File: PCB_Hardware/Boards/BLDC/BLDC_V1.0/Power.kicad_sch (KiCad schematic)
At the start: 43 parts, among them J3 Conn_01x02_Pin, J4 Conn_01x02_Pin, Q13 IPT015N10N5, Q2 IPT015N10N5, U11 AMS1117-3.3, U5 LM5069MM-2, U6 TLV70233_SOT23-5

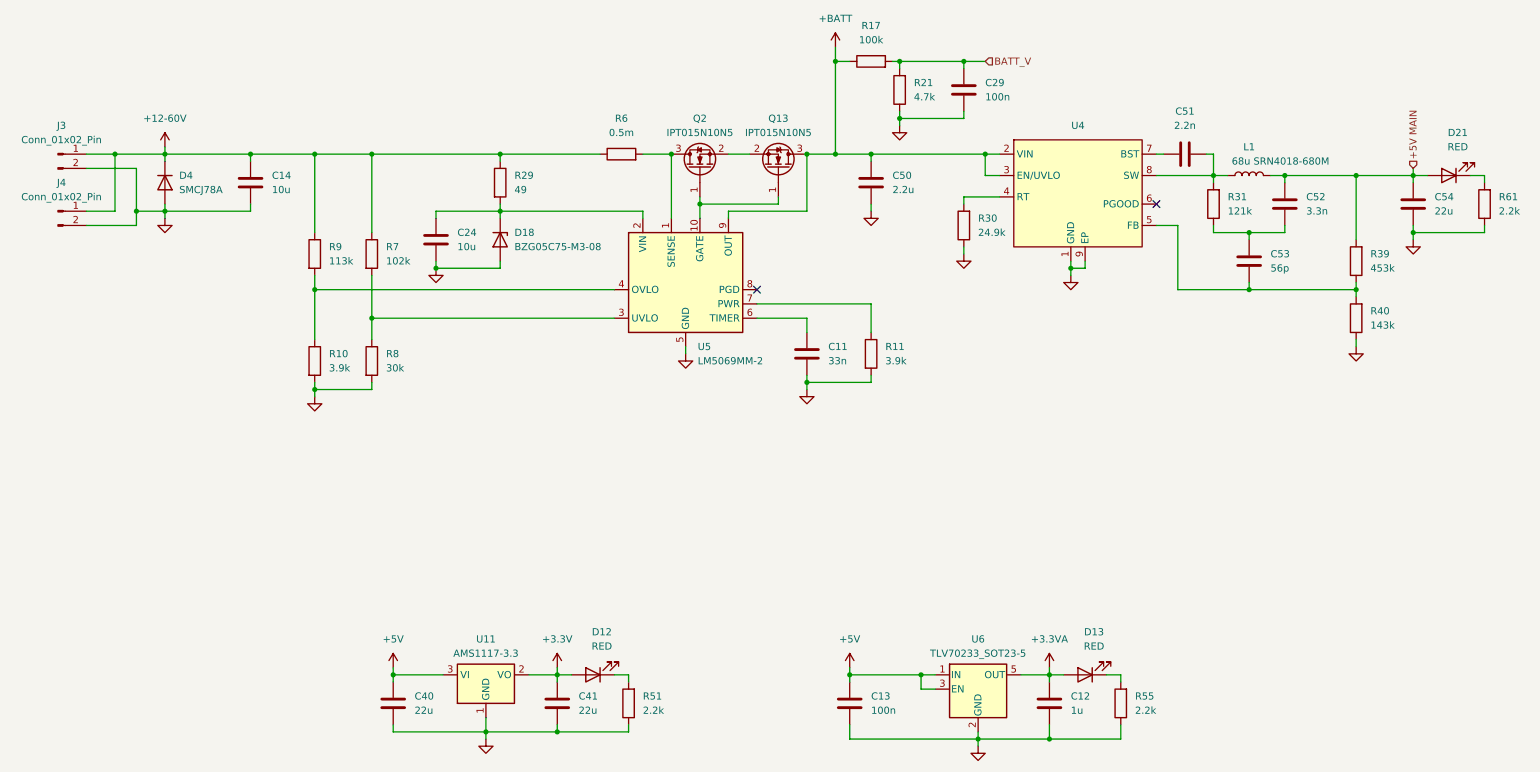
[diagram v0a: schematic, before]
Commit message: minor BLDC changes and production files for ordering
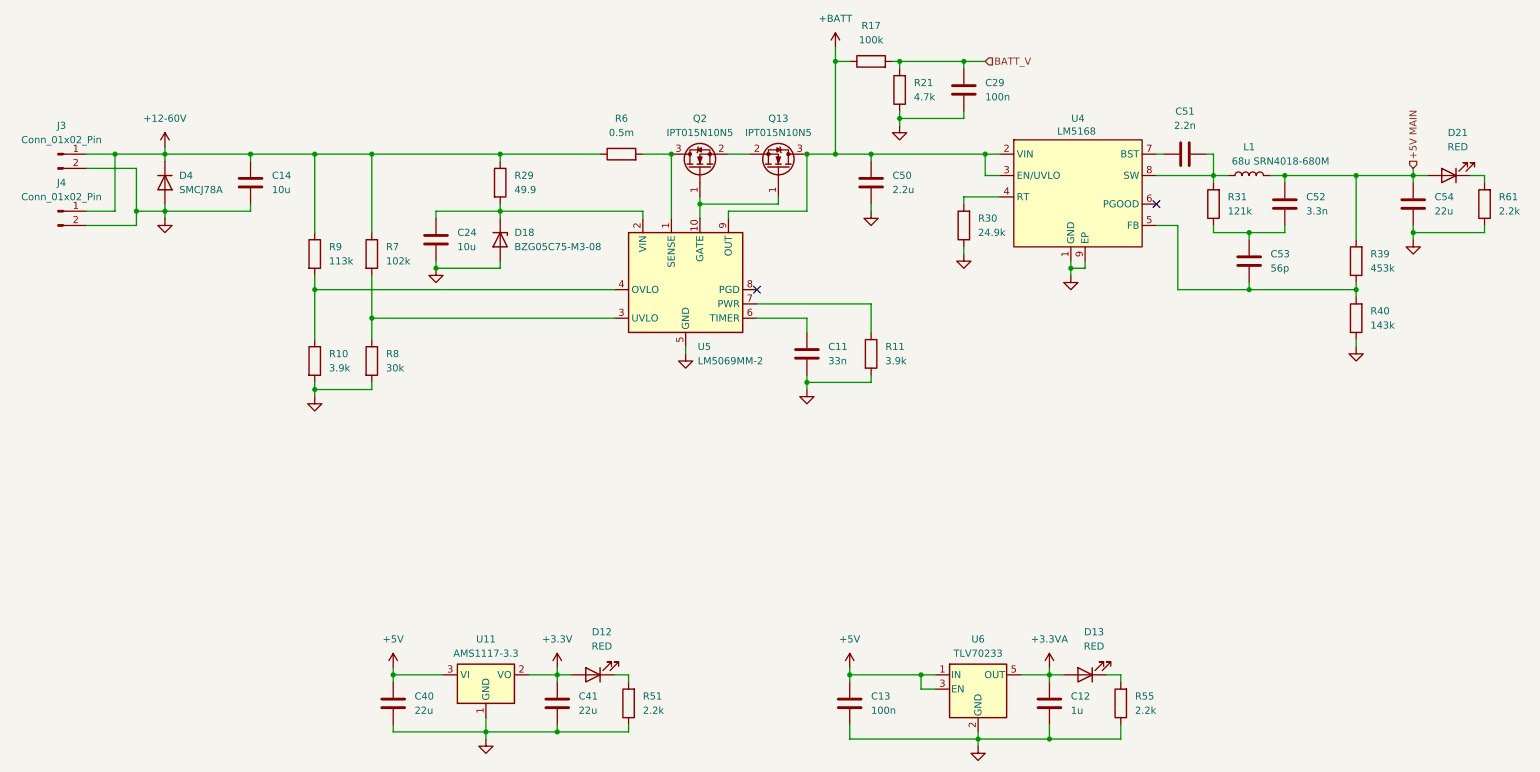
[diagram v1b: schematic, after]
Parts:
- C11: Manufacturer_Part_Number (none) -> CC0402MRX7R7BB333; Price (none) -> 0.0025
- C12: Manufacturer_Part_Number (none) -> CC0603ZRY5V6BB105; Price (none) -> 0.0065
- C13: Manufacturer_Part_Number (none) -> CC0402ZRY5V6BB104; Price (none) -> 0.0015
- C14, C24: Manufacturer_Part_Number (none) -> JMK107BJ106KA-T; Price (none) -> 0.0111
- C29: Manufacturer_Part_Number (none) -> GRM155R62A104KE14D; Price (none) -> 0.013
- C40, C41, C54: Manufacturer_Part_Number (none) -> CC0805KRX7R0BB681
- C50: Manufacturer_Part_Number (none) -> GRM21BD72A225ME01L
- C51: Manufacturer_Part_Number (none) -> CC0402MRX7R6BB222
- C52: Manufacturer_Part_Number (none) -> CC0402KRX7R7BB332
- C53: Manufacturer_Part_Number (none) -> CC0402GRNPO9BN560
- D12, D13, D21: Manufacturer_Part_Number (none) -> XINGLIGHT XL-1608SURC-06
- D18: Manufacturer_Part_Number (none) -> BZG05C75-M3-08
- J3, J4: Manufacturer_Part_Number (none) -> XT30PW-M30.G.Y
- L1: Manufacturer_Part_Number (none) -> SRN4018-680M
- Q13, Q2: Manufacturer_Part_Number (none) -> IPT015N10N5
- R10: Manufacturer_Part_Number (none) -> 0805W8J0392T5E
- R11: Manufacturer_Part_Number (none) -> CQ02WGF3901TCE
- R17: Manufacturer_Part_Number (none) -> CQ03WAJ0104T5E
- R21: Manufacturer_Part_Number (none) -> 0603WAF3032T5S
- R29: value 49 -> 49.9; Manufacturer_Part_Number (none) -> 0805W8F499JT5E
- R30: Manufacturer_Part_Number (none) -> RC0402FR-0724K9L
- R31: Manufacturer_Part_Number (none) -> 0402WGF1213TCE
- R39: Manufacturer_Part_Number (none) -> CRCW0402453KFKED
- R40: Manufacturer_Part_Number (none) -> 0402WGF1433TCE
- R51, R55, R61: Manufacturer_Part_Number (none) -> 0402WGJ0222TCE
- R6: Manufacturer_Part_Number (none) -> WSL2512L5000FEA18
- R7: Manufacturer_Part_Number (none) -> 0805W8F1023T5E
- R8: Manufacturer_Part_Number (none) -> 0805W8J0303T5E
- R9: Manufacturer_Part_Number (none) -> 0805W8F1133T5E
- U11: Manufacturer_Part_Number (none) -> AMS1117-3.3
- U4: value (none) -> LM5168; Manufacturer_Part_Number (none) -> LM5168
- U5: Manufacturer_Part_Number (none) -> LM5069MM-2
- U6: value TLV70233_SOT23-5 -> TLV70233; Manufacturer_Part_Number (none) -> TLV70233
